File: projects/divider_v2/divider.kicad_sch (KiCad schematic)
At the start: 4 parts

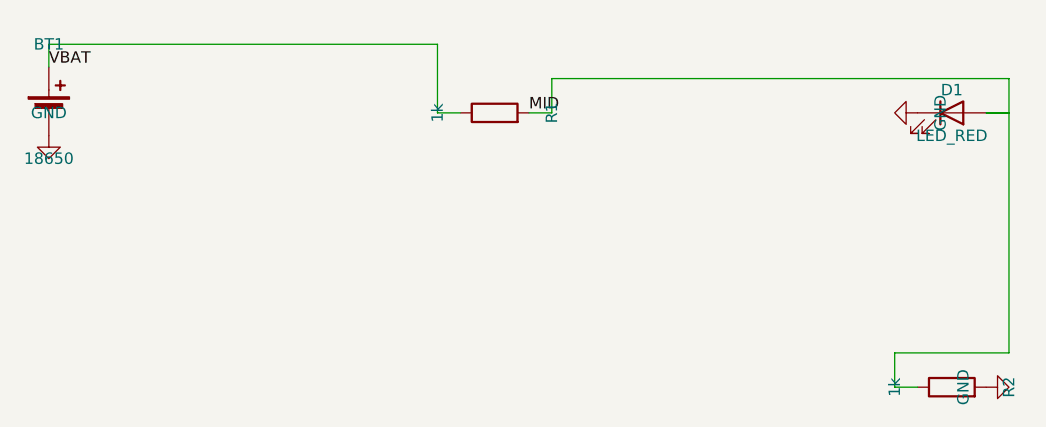
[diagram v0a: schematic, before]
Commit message: Phase 0: KiCad 10 migration + fix blind ERC parsing
- kicad-cli writes JSON reports only to -o file, never stdout; runner
  now uses a temp report file and real JSON decoding
- DetectKicadCLI exported and reused by render_sch and export_test
- KiCad 10 symbol renames (ATmega328-AU -> ATmega328-A) and pin
  numbers fixed in demos

Co-Authored-By: Claude Fable 5 <noreply@anthropic.com>
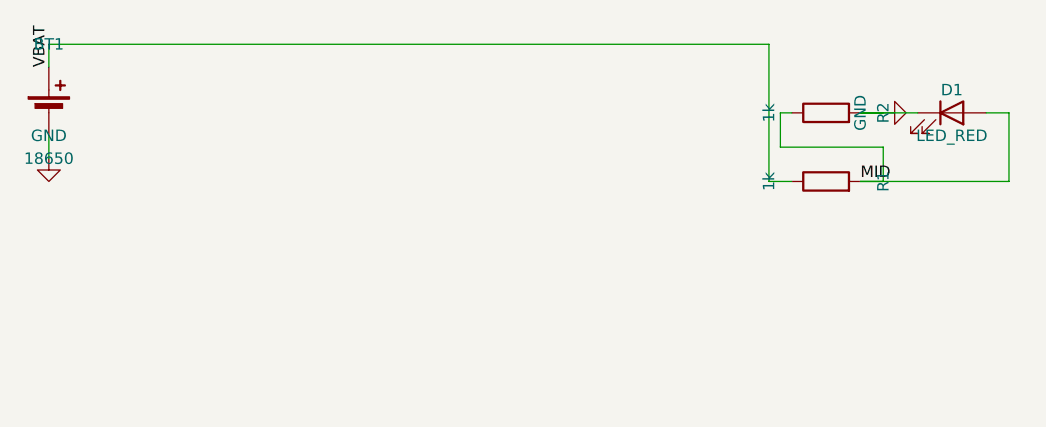
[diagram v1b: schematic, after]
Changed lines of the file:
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@@
     (instances
       (project ""
-        (path "/23a5284e-6881-4c21-8896-9c004b2bb089" (reference "BT1") (unit 1)))))
+        (path "/d4489af4-5a94-43f8-b35e-67bcd9e3d3c7" (reference "BT1") (unit 1)))))
   (symbol (lib_id "Device:R")
-    (at 100.33 50.8 90) (unit 1) (exclude_from_sim no) (in_bom yes) (on_board yes) (dnp no)
+    (at 137.16 58.42 90) (unit 1) (exclude_from_sim no) (in_bom yes) (on_board yes) (dnp no)
     (property "Reference" "R1"
-      (at 106.68 50.8 0)
+      (at 143.51 58.42 0)
       (effects
         (font (size 1.27 1.27))))
     (property "Value" "1k"
-      (at 93.98 50.8 0)
+      (at 130.81 58.42 0)
       (effects
         (font (size 1.27 1.27))))
     (property "Footprint" "Resistor_THT:R_Axial_DIN0207_L6.3mm_D2.5mm_P7.62mm_Horizontal"
-      (at 100.33 50.8 0)
+      (at 137.16 58.42 0)
       (effects
         (font (size 1.27 1.27)) (hide yes)))
     (property "Datasheet" ""
-      (at 100.33 50.8 0)
+      (at 137.16 58.42 0)
       (effects
         (font (size 1.27 1.27)) (hide yes)))
     (property "Description" ""
-      (at 100.33 50.8 0)
+      (at 137.16 58.42 0)
       (effects
         (font (size 1.27 1.27)) (hide yes)))
@@
     (instances
       (project ""
-        (path "/23a5284e-6881-4c21-8896-9c004b2bb089" (reference "R1") (unit 1)))))
+        (path "/d4489af4-5a94-43f8-b35e-67bcd9e3d3c7" (reference "R1") (unit 1)))))
   (symbol (lib_id "Device:R")
-    (at 151.13 81.28 90) (unit 1) (exclude_from_sim no) (in_bom yes) (on_board yes) (dnp no)
+    (at 137.16 50.8 90) (unit 1) (exclude_from_sim no) (in_bom yes) (on_board yes) (dnp no)
     (property "Reference" "R2"
-      (at 157.48 81.28 0)
+      (at 143.51 50.8 0)
       (effects
         (font (size 1.27 1.27))))
     (property "Value" "1k"
-      (at 144.78 81.28 0)
+      (at 130.81 50.8 0)
       (effects
         (font (size 1.27 1.27))))
     (property "Footprint" "Resistor_THT:R_Axial_DIN0207_L6.3mm_D2.5mm_P7.62mm_Horizontal"
-      (at 151.13 81.28 0)
+      (at 137.16 50.8 0)
       (effects
         (font (size 1.27 1.27)) (hide yes)))
     (property "Datasheet" ""
-      (at 151.13 81.28 0)
+      (at 137.16 50.8 0)
       (effects
         (font (size 1.27 1.27)) (hide yes)))
     (property "Description" ""
-      (at 151.13 81.28 0)
+      (at 137.16 50.8 0)
       (effects
         (font (size 1.27 1.27)) (hide yes)))
@@
     (instances
       (project ""
-        (path "/23a5284e-6881-4c21-8896-9c004b2bb089" (reference "R2") (unit 1)))))
+        (path "/d4489af4-5a94-43f8-b35e-67bcd9e3d3c7" (reference "R2") (unit 1)))))
   (symbol (lib_id "Device:LED")
     (at 151.13 50.8 0) (unit 1) (exclude_from_sim no) (in_bom yes) (on_board yes) (dnp no)
@@
     (instances
       (project ""
-        (path "/23a5284e-6881-4c21-8896-9c004b2bb089" (reference "D1") (unit 1)))))
+        (path "/d4489af4-5a94-43f8-b35e-67bcd9e3d3c7" (reference "D1") (unit 1)))))
   (wire
     (pts (xy 50.8 45.72) (xy 50.8 43.18))
     (stroke (width 0) (type default)))
   (wire
-    (pts (xy 50.8 43.18) (xy 93.98 43.18))
+    (pts (xy 50.8 43.18) (xy 130.81 43.18))
     (stroke (width 0) (type default)))
   (wire
-    (pts (xy 93.98 43.18) (xy 93.98 50.8))
+    (pts (xy 130.81 43.18) (xy 130.81 58.42))
     (stroke (width 0) (type default)))
   (wire
-    (pts (xy 93.98 50.8) (xy 96.52 50.8))
+    (pts (xy 130.81 58.42) (xy 133.35 58.42))
     (stroke (width 0) (type default)))
   (label "VBAT"
-    (at 50.8 45.72 0) (fields_autoplaced yes)
-    (effects
-      (font (size 1.27 1.27)) (justify left bottom))
-    (property "Intersheet References" ""
-      (at 0 0 0)
-      (effects
-        (font (size 1.27 1.27)) (hide yes))))
-  (wire
-    (pts (xy 104.14 50.8) (xy 106.68 50.8))
-    (stroke (width 0) (type default)))
-  (wire
-    (pts (xy 106.68 50.8) (xy 106.68 46.99))
-    (stroke (width 0) (type default)))
-  (wire
-    (pts (xy 106.68 46.99) (xy 157.48 46.99))
-    (stroke (width 0) (type default)))
-  (wire
-    (pts (xy 157.48 46.99) (xy 157.48 50.8))
-    (stroke (width 0) (type default)))
-  (wire
-    (pts (xy 157.48 50.8) (xy 154.94 50.8))
-    (stroke (width 0) (type default)))
-  (wire
-    (pts (xy 154.94 50.8) (xy 157.48 50.8))
-    (stroke (width 0) (type default)))
-  (wire
-    (pts (xy 157.48 50.8) (xy 157.48 77.47))
-    (stroke (width 0) (type default)))
-  (wire
-    (pts (xy 157.48 77.47) (xy 144.78 77.47))
-    (stroke (width 0) (type default)))
-  (wire
-    (pts (xy 144.78 77.47) (xy 144.78 81.28))
-    (stroke (width 0) (type default)))
-  (wire
-    (pts (xy 144.78 81.28) (xy 147.32 81.28))
-    (stroke (width 0) (type default)))
-  (label "MID"
-    (at 104.14 50.8 0) (fields_autoplaced yes)
+    (at 50.8 45.72 90) (fields_autoplaced yes)
     (effects
       (font (size 1.27 1.27)) (justify left bottom))
@@
         (font (size 1.27 1.27)) (hide yes))))
   (symbol (lib_id "power:GND")
-    (at 154.94 81.28 90) (unit 1) (exclude_from_sim no) (in_bom no) (on_board no) (dnp no)
+    (at 50.8 55.88 0) (unit 1) (exclude_from_sim no) (in_bom no) (on_board no) (dnp no)
     (property "Reference" "#PWR01"
-      (at 154.94 81.28 0)
+      (at 50.8 55.88 0)
       (effects
         (font (size 1.27 1.27)) (hide yes)))
     (property "Value" "GND"
-      (at 152.4 81.28 0)
+      (at 50.8 53.34 0)
       (effects
         (font (size 1.27 1.27))))
     (property "Footprint" ""
-      (at 154.94 81.28 0)
+      (at 50.8 55.88 0)
       (effects
         (font (size 1.27 1.27)) (hide yes)))
     (property "Datasheet" ""
-      (at 154.94 81.28 0)
+      (at 50.8 55.88 0)
       (effects
         (font (size 1.27 1.27)) (hide yes)))
     (property "Description" ""
-      (at 154.94 81.28 0)
+      (at 50.8 55.88 0)
       (effects
         (font (size 1.27 1.27)) (hide yes)))
@@
     (instances
       (project ""
-        (path "/23a5284e-6881-4c21-8896-9c004b2bb089" (reference "#PWR01") (unit 1)))))
+        (path "/d4489af4-5a94-43f8-b35e-67bcd9e3d3c7" (reference "#PWR01") (unit 1)))))
+  (wire
+    (pts (xy 50.8 53.34) (xy 50.8 55.88))
+    (stroke (width 0) (type default)))
+  (wire
+    (pts (xy 140.97 50.8) (xy 147.32 50.8))
+    (stroke (width 0) (type default)))
   (symbol (lib_id "power:GND")
-    (at 147.32 50.8 270) (unit 1) (exclude_from_sim no) (in_bom no) (on_board no) (dnp no)
+    (at 143.51 50.8 90) (unit 1) (exclude_from_sim no) (in_bom no) (on_board no) (dnp no)
     (property "Reference" "#PWR02"
-      (at 147.32 50.8 0)
+      (at 143.51 50.8 0)
       (effects
         (font (size 1.27 1.27)) (hide yes)))
     (property "Value" "GND"
-      (at 149.86 50.8 0)
+      (at 140.97 50.8 0)
       (effects
         (font (size 1.27 1.27))))
     (property "Footprint" ""
-      (at 147.32 50.8 0)
+      (at 143.51 50.8 0)
       (effects
         (font (size 1.27 1.27)) (hide yes)))
     (property "Datasheet" ""
-      (at 147.32 50.8 0)
+      (at 143.51 50.8 0)
       (effects
         (font (size 1.27 1.27)) (hide yes)))
     (property "Description" ""
-      (at 147.32 50.8 0)
+      (at 143.51 50.8 0)
       (effects
         (font (size 1.27 1.27)) (hide yes)))
@@
     (instances
       (project ""
-        (path "/23a5284e-6881-4c21-8896-9c004b2bb089" (reference "#PWR02") (unit 1)))))
-  (symbol (lib_id "power:GND")
-    (at 50.8 53.34 0) (unit 1) (exclude_from_sim no) (in_bom no) (on_board no) (dnp no)
-    (property "Reference" "#PWR03"
-      (at 50.8 53.34 0)
+        (path "/d4489af4-5a94-43f8-b35e-67bcd9e3d3c7" (reference "#PWR02") (unit 1)))))
+  (wire
+    (pts (xy 140.97 50.8) (xy 143.51 50.8))
+    (stroke (width 0) (type default)))
+  (wire
+    (pts (xy 140.97 58.42) (xy 143.51 58.42))
+    (stroke (width 0) (type default)))
+  (wire
+    (pts (xy 143.51 58.42) (xy 143.51 54.61))
+    (stroke (width 0) (type default)))
+  (wire
+    (pts (xy 143.51 54.61) (xy 132.08 54.61))
+    (stroke (width 0) (type default)))
+  (wire
+    (pts (xy 132.08 54.61) (xy 132.08 50.8))
+    (stroke (width 0) (type default)))
+  (wire
+    (pts (xy 132.08 50.8) (xy 133.35 50.8))
+    (stroke (width 0) (type default)))
+  (wire
+    (pts (xy 140.97 58.42) (xy 157.48 58.42))
+    (stroke (width 0) (type default)))
+  (wire
+    (pts (xy 157.48 58.42) (xy 157.48 50.8))
+    (stroke (width 0) (type default)))
+  (wire
+    (pts (xy 157.48 50.8) (xy 154.94 50.8))
+    (stroke (width 0) (type default)))
+  (label "MID"
+    (at 140.97 58.42 0) (fields_autoplaced yes)
+    (effects
+      (font (size 1.27 1.27)) (justify left bottom))
+    (property "Intersheet References" ""
+      (at 0 0 0)
       (effects
-        (font (size 1.27 1.27)) (hide yes)))
-    (property "Value" "GND"
-      (at 50.8 50.8 0)
-      (effects
-        (font (size 1.27 1.27))))
-    (property "Footprint" ""
-      (at 50.8 53.34 0)
-      (effects
-        (font (size 1.27 1.27)) (hide yes)))
-    (property "Datasheet" ""
-      (at 50.8 53.34 0)
-      (effects
-        (font (size 1.27 1.27)) (hide yes)))
-    (property "Description" ""
-      (at 50.8 53.34 0)
-      (effects
-        (font (size 1.27 1.27)) (hide yes)))
-    (pin "1")
-    (instances
-      (project ""
-        (path "/23a5284e-6881-4c21-8896-9c004b2bb089" (reference "#PWR03") (unit 1))))))
+        (font (size 1.27 1.27)) (hide yes)))))

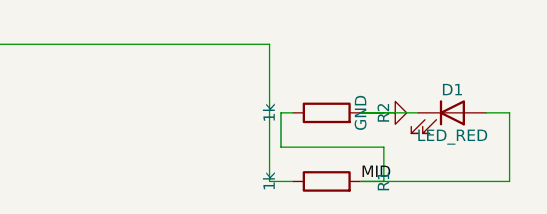
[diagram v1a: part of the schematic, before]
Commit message: Phase 1: geometric quality gate (internal/place2/gate)
Post-hoc Enforce() guarantees zero cross-net crossings, zero wires
through symbol bodies, zero collinear overlaps: offending nets are
demoted to net labels (no geometry, identical connectivity). Wired
into connect_netlist and relayout. Same-net duplicate segments are
merged by Clean, not demoted.

Co-Authored-By: Claude Fable 5 <noreply@anthropic.com>
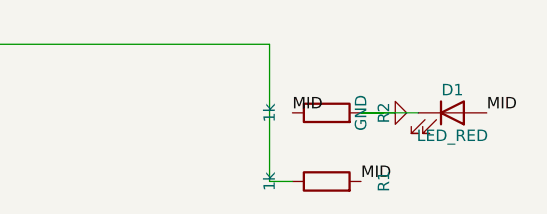
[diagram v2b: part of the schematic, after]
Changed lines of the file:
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@@
     (instances
       (project ""
-        (path "/d4489af4-5a94-43f8-b35e-67bcd9e3d3c7" (reference "BT1") (unit 1)))))
+        (path "/92e67ea4-57cd-45de-bb6b-c453c3c0f43a" (reference "BT1") (unit 1)))))
   (symbol (lib_id "Device:R")
     (at 137.16 58.42 90) (unit 1) (exclude_from_sim no) (in_bom yes) (on_board yes) (dnp no)
@@
     (instances
       (project ""
-        (path "/d4489af4-5a94-43f8-b35e-67bcd9e3d3c7" (reference "R1") (unit 1)))))
+        (path "/92e67ea4-57cd-45de-bb6b-c453c3c0f43a" (reference "R1") (unit 1)))))
   (symbol (lib_id "Device:R")
     (at 137.16 50.8 90) (unit 1) (exclude_from_sim no) (in_bom yes) (on_board yes) (dnp no)
@@
     (instances
       (project ""
-        (path "/d4489af4-5a94-43f8-b35e-67bcd9e3d3c7" (reference "R2") (unit 1)))))
+        (path "/92e67ea4-57cd-45de-bb6b-c453c3c0f43a" (reference "R2") (unit 1)))))
   (symbol (lib_id "Device:LED")
     (at 151.13 50.8 0) (unit 1) (exclude_from_sim no) (in_bom yes) (on_board yes) (dnp no)
@@
     (instances
       (project ""
-        (path "/d4489af4-5a94-43f8-b35e-67bcd9e3d3c7" (reference "D1") (unit 1)))))
+        (path "/92e67ea4-57cd-45de-bb6b-c453c3c0f43a" (reference "D1") (unit 1)))))
   (wire
     (pts (xy 50.8 45.72) (xy 50.8 43.18))
@@
     (instances
       (project ""
-        (path "/d4489af4-5a94-43f8-b35e-67bcd9e3d3c7" (reference "#PWR01") (unit 1)))))
+        (path "/92e67ea4-57cd-45de-bb6b-c453c3c0f43a" (reference "#PWR01") (unit 1)))))
   (wire
     (pts (xy 50.8 53.34) (xy 50.8 55.88))
@@
     (instances
       (project ""
-        (path "/d4489af4-5a94-43f8-b35e-67bcd9e3d3c7" (reference "#PWR02") (unit 1)))))
+        (path "/92e67ea4-57cd-45de-bb6b-c453c3c0f43a" (reference "#PWR02") (unit 1)))))
   (wire
     (pts (xy 140.97 50.8) (xy 143.51 50.8))
-    (stroke (width 0) (type default)))
-  (wire
-    (pts (xy 140.97 58.42) (xy 143.51 58.42))
-    (stroke (width 0) (type default)))
-  (wire
-    (pts (xy 143.51 58.42) (xy 143.51 54.61))
-    (stroke (width 0) (type default)))
-  (wire
-    (pts (xy 143.51 54.61) (xy 132.08 54.61))
-    (stroke (width 0) (type default)))
-  (wire
-    (pts (xy 132.08 54.61) (xy 132.08 50.8))
-    (stroke (width 0) (type default)))
-  (wire
-    (pts (xy 132.08 50.8) (xy 133.35 50.8))
-    (stroke (width 0) (type default)))
-  (wire
-    (pts (xy 140.97 58.42) (xy 157.48 58.42))
-    (stroke (width 0) (type default)))
-  (wire
-    (pts (xy 157.48 58.42) (xy 157.48 50.8))
-    (stroke (width 0) (type default)))
-  (wire
-    (pts (xy 157.48 50.8) (xy 154.94 50.8))
     (stroke (width 0) (type default)))
   (label "MID"
@@
     (effects
       (font (size 1.27 1.27)) (justify left bottom))
+    (property "Intersheet References" ""
+      (at 0 0 0)
+      (effects
+        (font (size 1.27 1.27)) (hide yes))))
+  (label "MID"
+    (at 133.35 50.8 0) (fields_autoplaced yes)
+    (effects
+      (font (size 1.27 1.27)) (justify left bottom))
+    (property "Intersheet References" ""
+      (at 0 0 0)
+      (effects
+        (font (size 1.27 1.27)) (hide yes))))
+  (label "MID"
+    (at 154.94 50.8 0) (fields_autoplaced yes)
+    (effects
+      (font (size 1.27 1.27)) (justify left bottom))
